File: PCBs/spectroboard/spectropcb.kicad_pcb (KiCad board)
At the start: 2 copper layers, 67.5 x 50 mm, 14 parts, among them J1 Conn_02x07_Odd_Even, J2 Conn_02x08_Odd_Even, J3 Conn_02x08_Odd_Even, J4 Conn_01x02_Pin, J6 SM04B-GHS-TB, Q1 2SA1015, U1 TCD1304DG, U2 SN74HC04N

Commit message: first thoughts
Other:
- board text added: "How big are these devices, the motherboard has an overhang past the jumpers, so if these are tall it could be an issue"
- board text added: "I would reccomend using a ground plane and vias instead of the ground traces, especially since most of the traces on the back are ground anyways"
- board text added: "Pretty jaggad traces, not a huge deal but there is space, so I'd change it"
- board text added: "This jumper is backwards"
- board text added: "this traces doesn't need to go around, it can just go straight to its destination, since its on the bottom"
- board text added: "use JST GH, not PH"
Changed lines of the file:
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@@
 		(layer "Edge.Cuts")
+	)
+	(gr_rect
+		(start 119.08 50.01)
+		(end 132.43 63.45)
+		(stroke
+			(width 0.1)
+			(type default)
+		)
+		(fill no)
+		(layer "User.1")
+	)
+	(gr_text "I would reccomend using a ground plane \nand vias instead of the ground traces, especially since most of the\ntraces on the back are ground anyways"
+		(at 146.08 41.93 0)
+		(layer "User.1")
+		(effects
+			(font
+				(size 1 1)
+				(thickness 0.15)
+			)
+			(justify left bottom)
+		)
+	)
+	(gr_text "This jumper is backwards"
+		(at 127.4 93.98 0)
+		(layer "User.1")
+		(effects
+			(font
+				(size 0.5 0.5)
+				(thickness 0.125)
+				(bold yes)
+			)
+			(justify left bottom)
+		)
+	)
+	(gr_text "use JST GH, not PH"
+		(at 146.99 89.89 0)
+		(layer "User.1")
+		(effects
+			(font
+				(size 0.5 0.5)
+				(thickness 0.125)
+				(bold yes)
+			)
+			(justify left bottom)
+		)
+	)
+	(gr_text "this traces doesn't need to go around, \nit can just go straight to its \ndestination, since its on the bottom\n"
+		(at 122.06 66.63 270)
+		(layer "User.1")
+		(effects
+			(font
+				(size 0.5 0.5)
+				(thickness 0.125)
+				(bold yes)
+			)
+			(justify left bottom)
+		)
+	)
+	(gr_text "Pretty jaggad traces,\nnot a huge deal but there\nis space, so I'd change it"
+		(at 119.08 54.54 0)
+		(layer "User.1")
+		(effects
+			(font
+				(size 1 1)
+				(thickness 0.15)
+			)
+			(justify left bottom)
+		)
+	)
+	(gr_text "How big are these devices, the \nmotherboard has an overhang past\nthe jumpers, so if these are tall\nit could be an issue"
+		(at 160.67 56.37 0)
+		(layer "User.1")
+		(effects
+			(font
+				(size 1 1)
+				(thickness 0.15)
+			)
+			(justify left bottom)
+		)
 	)
 	(segment

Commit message: updated pcb
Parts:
- J4: footprint Connector_JST:JST_PH_B2B-PH-K_1x02_P2.00mm_Vertical -> Connector_JST:JST_GH_SM02B-GHS-TB_1x02-1MP_P1.25mm_Horizontal
- moved J6 3.54 mm to (127.5, 85.0), turned to 0 degrees
- moved R2 1.88 mm to (157.5, 58.9), turned to 90 degrees
- moved U2 1.88 mm to (161.0, 73.9)
- moved U1 1.56 mm to (178.5, 54.6)
- moved C2 0.80 mm to (152.7, 67.5)
- moved C3 0.80 mm to (150.2, 65.0)
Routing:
- net GND: track 232.9 -> 14.1 mm, vias 0 -> 6
- net Net-(Q1-B): track 58.3 -> 27.1 mm
- net /21: track 57.8 -> 34.3 mm
- net /17: track 33.0 -> 13.5 mm
- net +5V: track 185.8 -> 180.6 mm
- net Net-(U1-OS): track 14.9 -> 11.2 mm
- net /16: track 23.3 -> 19.9 mm
- net /39: track 21.3 -> 19.3 mm
- net Net-(Q1-C): track 8.00 -> 7.09 mm
- net Net-(U1-phiM): track 26.9 -> 26.4 mm
- added copper zone on B.Cu, net GND
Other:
- board size 67.5 x 50 mm -> 60 x 45 mm
- board text removed: "How big are these devices, the motherboard has an overhang past the jumpers, so if these are tall it could be an issue"
- board text removed: "I would reccomend using a ground plane and vias instead of the ground traces, especially since most of the traces on the back are ground anyways"
- board text removed: "Pretty jaggad traces, not a huge deal but there is space, so I'd change it"
- board text removed: "This jumper is backwards"
- board text removed: "this traces doesn't need to go around, it can just go straight to its destination, since its on the bottom"
- board text removed: "use JST GH, not PH"

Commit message: pinout checked, silkscreen added
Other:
- board text added: "+5V"
- board text added: "GND"
- board text added: "PWM"
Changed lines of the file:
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@@
 		(layer "Edge.Cuts")
+	)
+	(gr_text "PWM"
+		(at 126.07 88.96 0)
+		(layer "F.SilkS")
+		(effects
+			(font
+				(size 1 1)
+				(thickness 0.1)
+			)
+			(justify left bottom)
+		)
+	)
+	(gr_text "GND"
+		(at 148.48 88.92 0)
+		(layer "F.SilkS")
+		(effects
+			(font
+				(size 1 1)
+				(thickness 0.1)
+			)
+			(justify left bottom)
+		)
+	)
+	(gr_text "+5V"
+		(at 144.47 89.03 0)
+		(layer "F.SilkS")
+		(effects
+			(font
+				(size 1 1)
+				(thickness 0.1)
+			)
+			(justify left bottom)
+		)
+	)
+	(gr_text "GND"
+		(at 129.48 89.08 0)
+		(layer "F.SilkS")
+		(effects
+			(font
+				(size 1 1)
+				(thickness 0.1)
+			)
+			(justify left bottom)
+		)
+	)
+	(gr_text "+5V"
+		(at 122.95 89.08 0)
+		(layer "F.SilkS")
+		(effects
+			(font
+				(size 1 1)
+				(thickness 0.1)
+			)
+			(justify left bottom)
+		)
 	)
 	(segment

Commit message: mounting holes
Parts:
- added H1: MountingHole, MountingHole:MountingHole_3.2mm_M3, F.Cu at (127.5, 50.0)
- added H2: MountingHole, MountingHole:MountingHole_3.2mm_M3, F.Cu at (163.0, 50.4)
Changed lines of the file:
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@@
+		(embedded_fonts no)
+	)
+	(footprint "MountingHole:MountingHole_3.2mm_M3"
+		(layer "F.Cu")
+		(at 163.04 50.39)
+		(descr "Mounting Hole 3.2mm, M3, no annular, generated by kicad-footprint-generator mountinghole.py")
+		(tags "mountinghole M3")
+		(property "Reference" "H2"
+			(at 0 -4.15 0)
+			(layer "F.SilkS")
+			(effects
+				(font
+					(size 1 1)
+					(thickness 0.15)
+				)
+			)
+		)
+		(property "Value" "MountingHole"
+			(at 0 4.15 0)
+			(layer "F.Fab")
+			(effects
+				(font
+					(size 1 1)
+					(thickness 0.15)
+				)
+			)
+		)
+		(property "Datasheet" "~"
+			(at 0 0 0)
+			(layer "F.Fab")
+			(hide yes)
+			(effects
+				(font
+					(size 1.27 1.27)
+					(thickness 0.15)
+				)
+			)
+		)
+		(property "Description" "Mounting Hole without connection"
+			(at 0 0 0)
+			(layer "F.Fab")
+			(hide yes)
+			(effects
+				(font
+					(size 1.27 1.27)
+					(thickness 0.15)
+				)
+			)
+		)
+		(property ki_fp_filters "MountingHole*")
+		(sheetname "/")
+		(sheetfile "spectropcb.kicad_sch")
+		(attr exclude_from_pos_files exclude_from_bom)
+		(fp_circle
+			(center 0 0)
+			(end 3.2 0)
+			(stroke
+				(width 0.15)
+				(type solid)
+			)
+			(fill no)
+			(layer "Cmts.User")
+		)
+		(fp_circle
+			(center 0 0)
+			(end 3.45 0)
+			(stroke
+				(width 0.05)
+				(type solid)
+			)
+			(fill no)
+			(layer "F.CrtYd")
+		)
+		(fp_text user "${REFERENCE}"
+			(at 0 0 0)
+			(layer "F.Fab")
+			(effects
+				(font
+					(size 1 1)
+					(thickness 0.15)
+				)
+			)
+		)
+		(pad "" np_thru_hole circle
+			(at 0 -0.43)
+			(size 3.2 3.2)
+			(drill 3.2)
+			(layers "*.Cu" "*.Mask")
+		)
 		(embedded_fonts no)
 	)
@@
 		)
 	)
+	(footprint "MountingHole:MountingHole_3.2mm_M3"
+		(layer "F.Cu")
+		(at 127.53 49.96)
+		(descr "Mounting Hole 3.2mm, M3, no annular, generated by kicad-footprint-generator mountinghole.py")
+		(tags "mountinghole M3")
+		(property "Reference" "H1"
+			(at 0 -4.15 0)
+			(layer "F.SilkS")
+			(effects
+				(font
+					(size 1 1)
+					(thickness 0.15)
+				)
+			)
+		)
+		(property "Value" "MountingHole"
+			(at 0 4.15 0)
+			(layer "F.Fab")
+			(effects
+				(font
+					(size 1 1)
+					(thickness 0.15)
+				)
+			)
+		)
+		(property "Datasheet" "~"
+			(at 0 0 0)
+			(layer "F.Fab")
+			(hide yes)
+			(effects
+				(font
+					(size 1.27 1.27)
+					(thickness 0.15)
+				)
+			)
+		)
+		(property "Description" "Mounting Hole without connection"
+			(at 0 0 0)
+			(layer "F.Fab")
+			(hide yes)
+			(effects
+				(font
+					(size 1.27 1.27)
+					(thickness 0.15)
+				)
+			)
+		)
+		(property ki_fp_filters "MountingHole*")
+		(sheetname "/")
+		(sheetfile "spectropcb.kicad_sch")
+		(attr exclude_from_pos_files exclude_from_bom)
+		(fp_circle
+			(center 0 0)
+			(end 3.2 0)
+			(stroke
+				(width 0.15)
+				(type solid)
+			)
+			(fill no)
+			(layer "Cmts.User")
+		)
+		(fp_circle
+			(center 0 0)
+			(end 3.45 0)
+			(stroke
+				(width 0.05)
+				(type solid)
+			)
+			(fill no)
+			(layer "F.CrtYd")
+		)
+		(fp_text user "${REFERENCE}"
+			(at 0 0 0)
+			(layer "F.Fab")
+			(effects
+				(font
+					(size 1 1)
+					(thickness 0.15)
+				)
+			)
+		)
+		(pad "" np_thru_hole circle
+			(at 0 0)
+			(size 3.2 3.2)
+			(drill 3.2)
+			(layers "*.Cu" "*.Mask")
+		)
+		(embedded_fonts no)
+	)
 	(footprint "Capacitor_SMD:C_1206_3216Metric"

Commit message: grounded ccd
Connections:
- U1 pad 10: unconnected-(U1-NC-Pad10) -> GND
- U1 pad 11: unconnected-(U1-NC-Pad11) -> GND
- U1 pad 12: unconnected-(U1-NC-Pad12) -> GND
- U1 pad 13: unconnected-(U1-NC-Pad13) -> GND
- U1 pad 14: unconnected-(U1-NC-Pad14) -> GND
- U1 pad 15: unconnected-(U1-NC-Pad15) -> GND
- U1 pad 16: unconnected-(U1-NC-Pad16) -> GND
- U1 pad 17: unconnected-(U1-NC-Pad17) -> GND
- U1 pad 18: unconnected-(U1-NC-Pad18) -> GND
- U1 pad 19: unconnected-(U1-NC-Pad19) -> GND
- U1 pad 20: unconnected-(U1-NC-Pad20) -> GND
- U1 pad 6: unconnected-(U1-NC-Pad6) -> GND
- U1 pad 7: unconnected-(U1-NC-Pad7) -> GND
- U1 pad 8: unconnected-(U1-NC-Pad8) -> GND
- U1 pad 9: unconnected-(U1-NC-Pad9) -> GND
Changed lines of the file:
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@@
 	(net 52 "Net-(U1-phiM)")
 	(net 53 "Net-(U1-ICG)")
-	(net 54 "unconnected-(U1-NC-Pad18)")
-	(net 55 "unconnected-(U1-NC-Pad15)")
-	(net 56 "unconnected-(U1-NC-Pad7)")
-	(net 57 "unconnected-(U1-NC-Pad11)")
-	(net 58 "unconnected-(U1-NC-Pad13)")
-	(net 59 "unconnected-(U1-NC-Pad19)")
-	(net 60 "unconnected-(U1-NC-Pad9)")
-	(net 61 "unconnected-(U1-NC-Pad20)")
-	(net 62 "unconnected-(U1-NC-Pad8)")
-	(net 63 "unconnected-(U1-NC-Pad16)")
-	(net 64 "unconnected-(U1-NC-Pad10)")
-	(net 65 "unconnected-(U1-NC-Pad14)")
-	(net 66 "Net-(U1-SH)")
-	(net 67 "unconnected-(U1-NC-Pad17)")
-	(net 68 "unconnected-(U1-NC-Pad12)")
-	(net 69 "unconnected-(U1-NC-Pad6)")
-	(net 70 "unconnected-(U2-5A-Pad11)")
-	(net 71 "unconnected-(U2-5Y-Pad10)")
-	(net 72 "unconnected-(U2-6A-Pad13)")
-	(net 73 "unconnected-(U2-4Y-Pad8)")
-	(net 74 "unconnected-(U2-6Y-Pad12)")
-	(net 75 "unconnected-(U2-4A-Pad9)")
+	(net 54 "Net-(U1-SH)")
+	(net 55 "unconnected-(U2-5A-Pad11)")
+	(net 56 "unconnected-(U2-5Y-Pad10)")
+	(net 57 "unconnected-(U2-6A-Pad13)")
+	(net 58 "unconnected-(U2-4Y-Pad8)")
+	(net 59 "unconnected-(U2-6Y-Pad12)")
+	(net 60 "unconnected-(U2-4A-Pad9)")
 	(footprint "Capacitor_SMD:C_0805_2012Metric"
 		(layer "F.Cu")
@@
 			(layers "*.Cu" "*.Mask")
 			(remove_unused_layers no)
-			(net 66 "Net-(U1-SH)")
+			(net 54 "Net-(U1-SH)")
 			(pinfunction "3Y")
 			(pintype "output")
@@
 			(layers "*.Cu" "*.Mask")
 			(remove_unused_layers no)
-			(net 73 "unconnected-(U2-4Y-Pad8)")
+			(net 58 "unconnected-(U2-4Y-Pad8)")
 			(pinfunction "4Y")
 			(pintype "output+no_connect")
@@
 			(layers "*.Cu" "*.Mask")
 			(remove_unused_layers no)
-			(net 75 "unconnected-(U2-4A-Pad9)")
+			(net 60 "unconnected-(U2-4A-Pad9)")
 			(pinfunction "4A")
 			(pintype "input+no_connect")
@@
 			(layers "*.Cu" "*.Mask")
 			(remove_unused_layers no)
-			(net 71 "unconnected-(U2-5Y-Pad10)")
+			(net 56 "unconnected-(U2-5Y-Pad10)")
 			(pinfunction "5Y")
 			(pintype "output+no_connect")
@@
 			(layers "*.Cu" "*.Mask")
 			(remove_unused_layers no)
-			(net 70 "unconnected-(U2-5A-Pad11)")
+			(net 55 "unconnected-(U2-5A-Pad11)")
 			(pinfunction "5A")
 			(pintype "input+no_connect")
@@
 			(layers "*.Cu" "*.Mask")
 			(remove_unused_layers no)
-			(net 74 "unconnected-(U2-6Y-Pad12)")
+			(net 59 "unconnected-(U2-6Y-Pad12)")
 			(pinfunction "6Y")
 			(pintype "output+no_connect")
@@
 			(layers "*.Cu" "*.Mask")
 			(remove_unused_layers no)
-			(net 72 "unconnected-(U2-6A-Pad13)")
+			(net 57 "unconnected-(U2-6A-Pad13)")
 			(pinfunction "6A")
 			(pintype "input+no_connect")
@@
 			(layers "*.Cu" "*.Mask")
 			(remove_unused_layers no)
-			(net 66 "Net-(U1-SH)")
+			(net 54 "Net-(U1-SH)")
 			(pinfunction "SH")
 			(pintype "unspecified")
@@
 			(layers "*.Cu" "*.Mask")
 			(remove_unused_layers no)
-			(net 69 "unconnected-(U1-NC-Pad6)")
+			(net 15 "GND")
 			(pinfunction "NC")
-			(pintype "no_connect")
+			(pintype "unspecified")
 		)
 		(pad "7" thru_hole circle
@@
 			(layers "*.Cu" "*.Mask")
 			(remove_unused_layers no)
-			(net 56 "unconnected-(U1-NC-Pad7)")
+			(net 15 "GND")
 			(pinfunction "NC")
-			(pintype "no_connect")
+			(pintype "unspecified")
 		)
 		(pad "8" thru_hole circle
@@
 			(layers "*.Cu" "*.Mask")
 			(remove_unused_layers no)
-			(net 62 "unconnected-(U1-NC-Pad8)")
+			(net 15 "GND")
 			(pinfunction "NC")
-			(pintype "no_connect")
+			(pintype "unspecified")
 		)
 		(pad "9" thru_hole circle
@@
 			(layers "*.Cu" "*.Mask")
 			(remove_unused_layers no)
-			(net 60 "unconnected-(U1-NC-Pad9)")
+			(net 15 "GND")
 			(pinfunction "NC")
-			(pintype "no_connect")
+			(pintype "unspecified")
 		)
 		(pad "10" thru_hole circle
@@
 			(layers "*.Cu" "*.Mask")
 			(remove_unused_layers no)
-			(net 64 "unconnected-(U1-NC-Pad10)")
+			(net 15 "GND")
 			(pinfunction "NC")
-			(pintype "no_connect")
+			(pintype "unspecified")
 		)
 		(pad "11" thru_hole circle
@@
 			(layers "*.Cu" "*.Mask")
 			(remove_unused_layers no)
-			(net 57 "unconnected-(U1-NC-Pad11)")
+			(net 15 "GND")
 			(pinfunction "NC")
-			(pintype "no_connect")
+			(pintype "unspecified")
 		)
 		(pad "12" thru_hole circle
@@
 			(layers "*.Cu" "*.Mask")
 			(remove_unused_layers no)
-			(net 68 "unconnected-(U1-NC-Pad12)")
+			(net 15 "GND")
 			(pinfunction "NC")
-			(pintype "no_connect")
+			(pintype "unspecified")
 		)
 		(pad "13" thru_hole circle
@@
 			(layers "*.Cu" "*.Mask")
 			(remove_unused_layers no)
-			(net 58 "unconnected-(U1-NC-Pad13)")
+			(net 15 "GND")
 			(pinfunction "NC")
-			(pintype "no_connect")
+			(pintype "unspecified")
 		)
 		(pad "14" thru_hole circle
@@
 			(layers "*.Cu" "*.Mask")
 			(remove_unused_layers no)
-			(net 65 "unconnected-(U1-NC-Pad14)")
+			(net 15 "GND")
 			(pinfunction "NC")
-			(pintype "no_connect")
+			(pintype "unspecified")
 		)
 		(pad "15" thru_hole circle
@@
 			(layers "*.Cu" "*.Mask")
 			(remove_unused_layers no)
-			(net 55 "unconnected-(U1-NC-Pad15)")
+			(net 15 "GND")
 			(pinfunction "NC")
-			(pintype "no_connect")
+			(pintype "unspecified")
 		)
 		(pad "16" thru_hole circle
@@
 			(layers "*.Cu" "*.Mask")
 			(remove_unused_layers no)
-			(net 63 "unconnected-(U1-NC-Pad16)")
+			(net 15 "GND")
 			(pinfunction "NC")
-			(pintype "no_connect")
+			(pintype "unspecified")
 		)
 		(pad "17" thru_hole circle
@@
 			(layers "*.Cu" "*.Mask")
 			(remove_unused_layers no)
-			(net 67 "unconnected-(U1-NC-Pad17)")
+			(net 15 "GND")
 			(pinfunction "NC")
-			(pintype "no_connect")
+			(pintype "unspecified")
 		)
 		(pad "18" thru_hole circle
@@
 			(layers "*.Cu" "*.Mask")
 			(remove_unused_layers no)
-			(net 54 "unconnected-(U1-NC-Pad18)")
+			(net 15 "GND")
 			(pinfunction "NC")
-			(pintype "no_connect")
+			(pintype "unspecified")
 		)
 		(pad "19" thru_hole circle
@@
 			(layers "*.Cu" "*.Mask")
 			(remove_unused_layers no)
-			(net 59 "unconnected-(U1-NC-Pad19)")
+			(net 15 "GND")
 			(pinfunction "NC")
-			(pintype "no_connect")
+			(pintype "unspecified")
 		)
 		(pad "20" thru_hole circle
@@
 			(layers "*.Cu" "*.Mask")
 			(remove_unused_layers no)
-			(net 61 "unconnected-(U1-NC-Pad20)")
+			(net 15 "GND")
 			(pinfunction "NC")
-			(pintype "no_connect")
+			(pintype "unspecified")
 		)
 		(pad "21" thru_hole circle
@@
 		(width 0.2)
 		(layer "F.Cu")
-		(net 66)
+		(net 54)
 	)
 	(segment
@@
 		(width 0.2)
 		(layer "F.Cu")
-		(net 66)
+		(net 54)
 	)
 	(segment
@@
 		(width 0.2)
 		(layer "F.Cu")
-		(net 66)
+		(net 54)
 	)
 	(segment
@@
 		(width 0.2)
 		(layer "F.Cu")
-		(net 66)
+		(net 54)
 	)
 	(zone

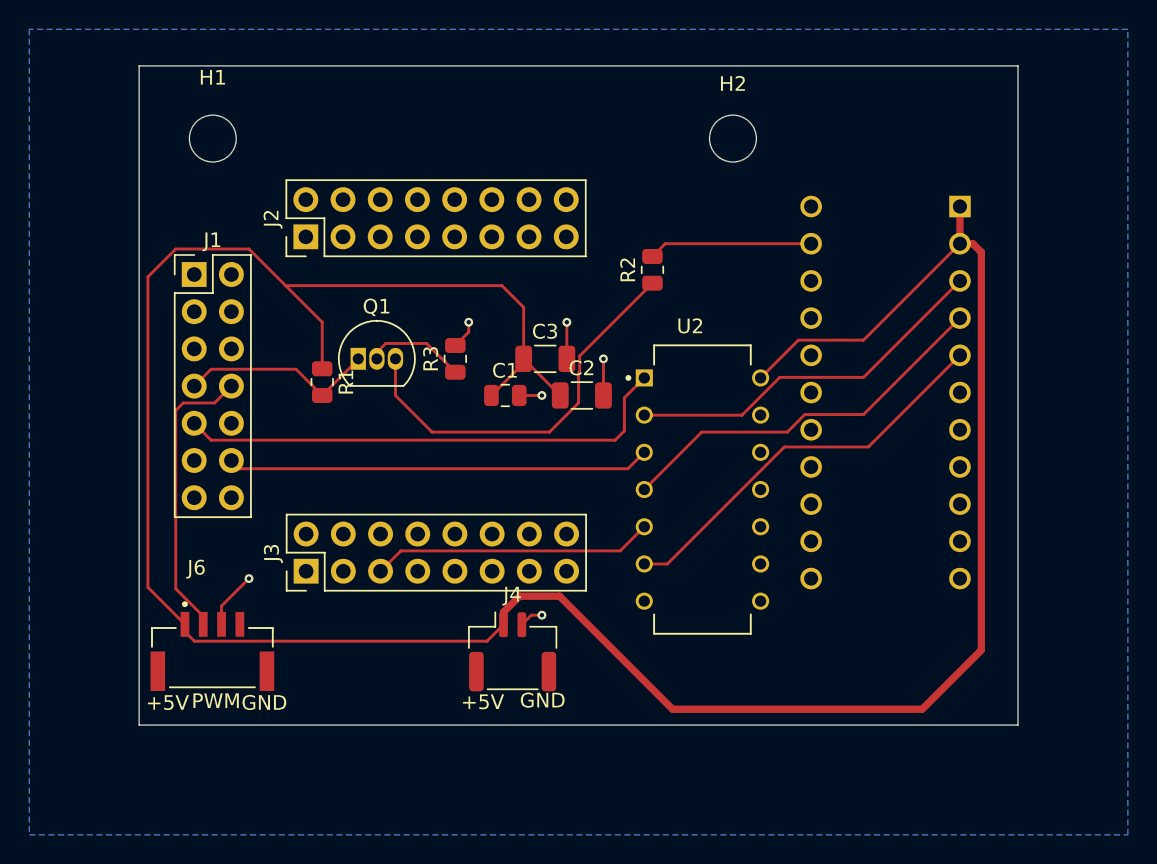
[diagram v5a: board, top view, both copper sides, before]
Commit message: 4 mounts
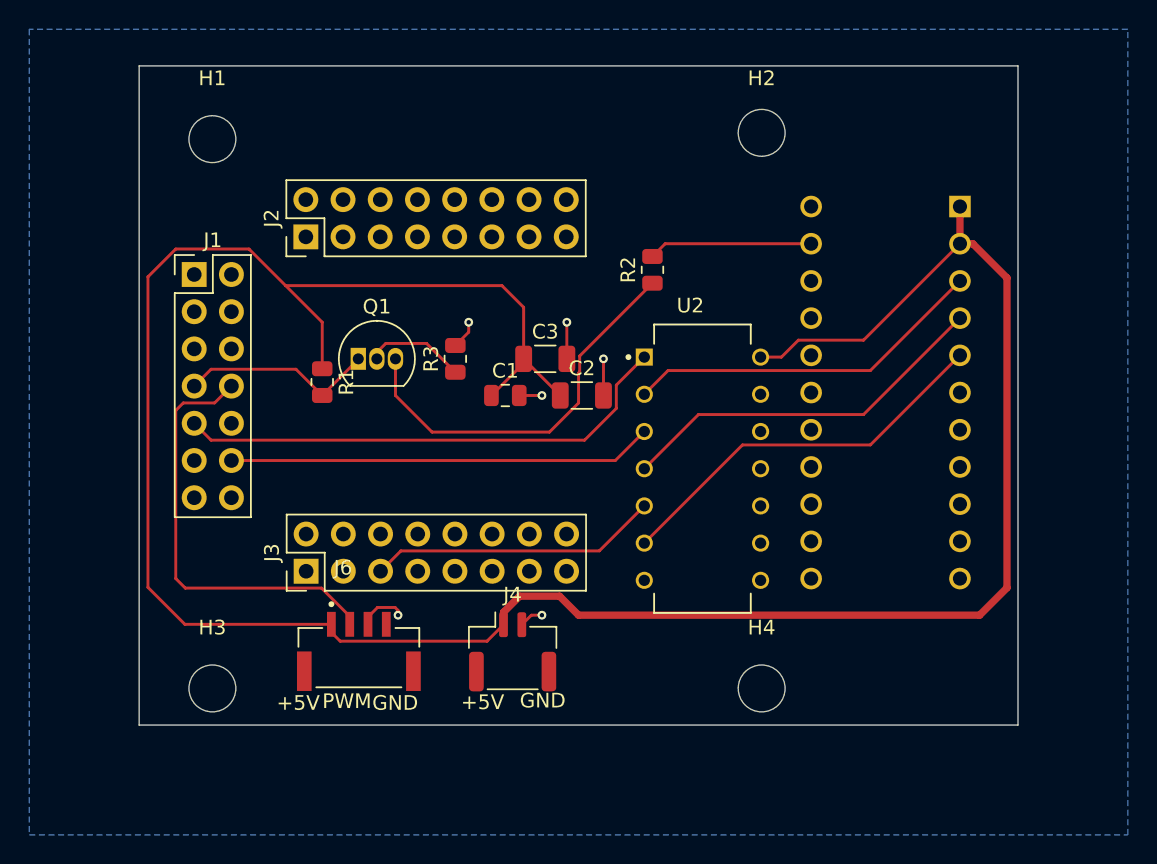
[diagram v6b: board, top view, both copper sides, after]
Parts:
- added H3: MountingHole, MountingHole:MountingHole_3.2mm_M3, F.Cu at (127.5, 87.5)
- added H4: MountingHole, MountingHole:MountingHole_3.2mm_M3, F.Cu at (165.0, 87.5)
- moved J6 10.0 mm to (137.5, 85.0)
- moved H2 2.00 mm to (165.0, 50.0)
- moved U2 1.42 mm to (161.0, 72.5)
- moved H1 0.05 mm to (127.5, 50.0)
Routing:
- net /16: track 19.9 -> 29.5 mm
- net +5V: track 180.6 -> 174.7 mm
- net GND: track 14.1 -> 13.4 mm
- net Net-(U1-SH): track 27.4 -> 26.9 mm
- net Net-(U1-ICG): track 25.3 -> 24.8 mm
- net Net-(U1-phiM): track 26.4 -> 25.8 mm
- net /39: track 19.3 -> 19.9 mm
